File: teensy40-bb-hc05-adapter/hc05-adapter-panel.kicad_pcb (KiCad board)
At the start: 2 copper layers, 90.2 x 101.9 mm, 402 parts, among them J1 Conn_01x06_0.1_Header, J2 Conn_01x06_0.1_Socket, U1 74LVC1G17, U2 74LVC1G14

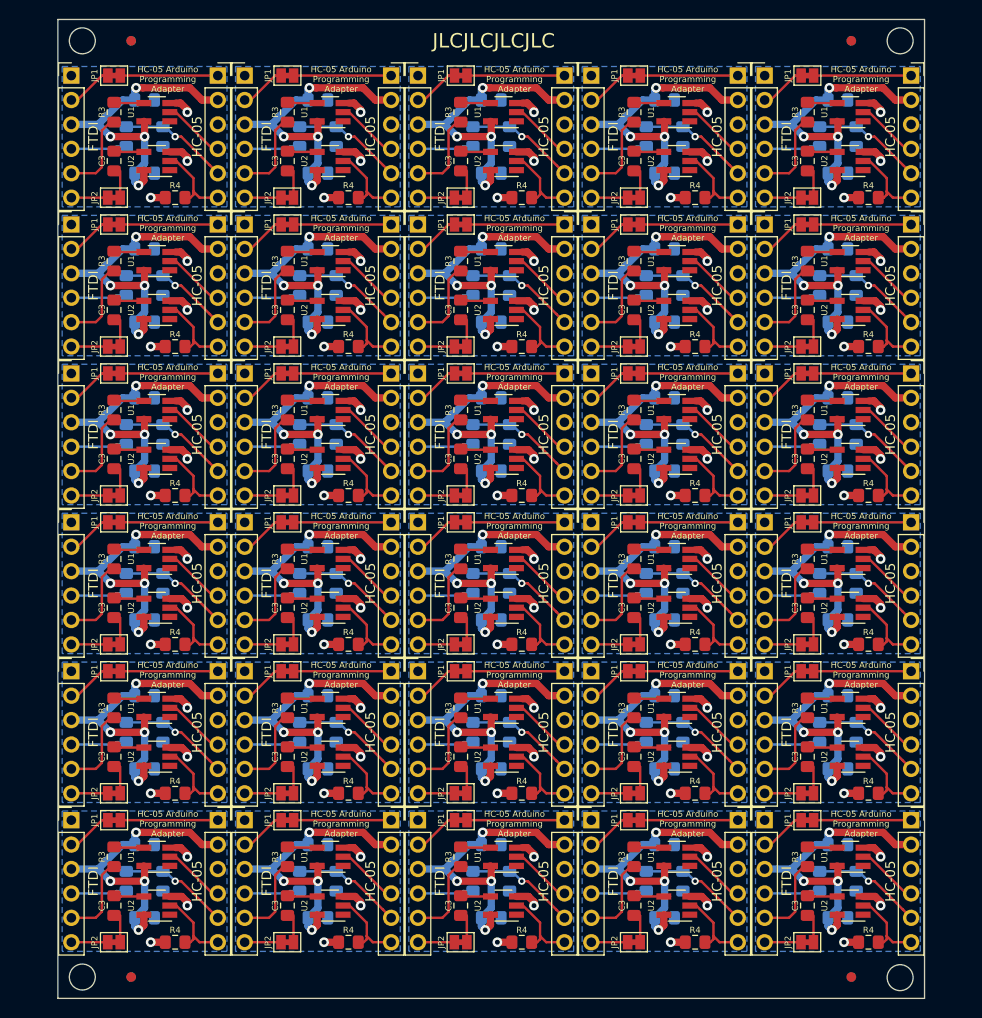
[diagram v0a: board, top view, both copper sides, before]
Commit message: Move edge rail to make less than 100mm long
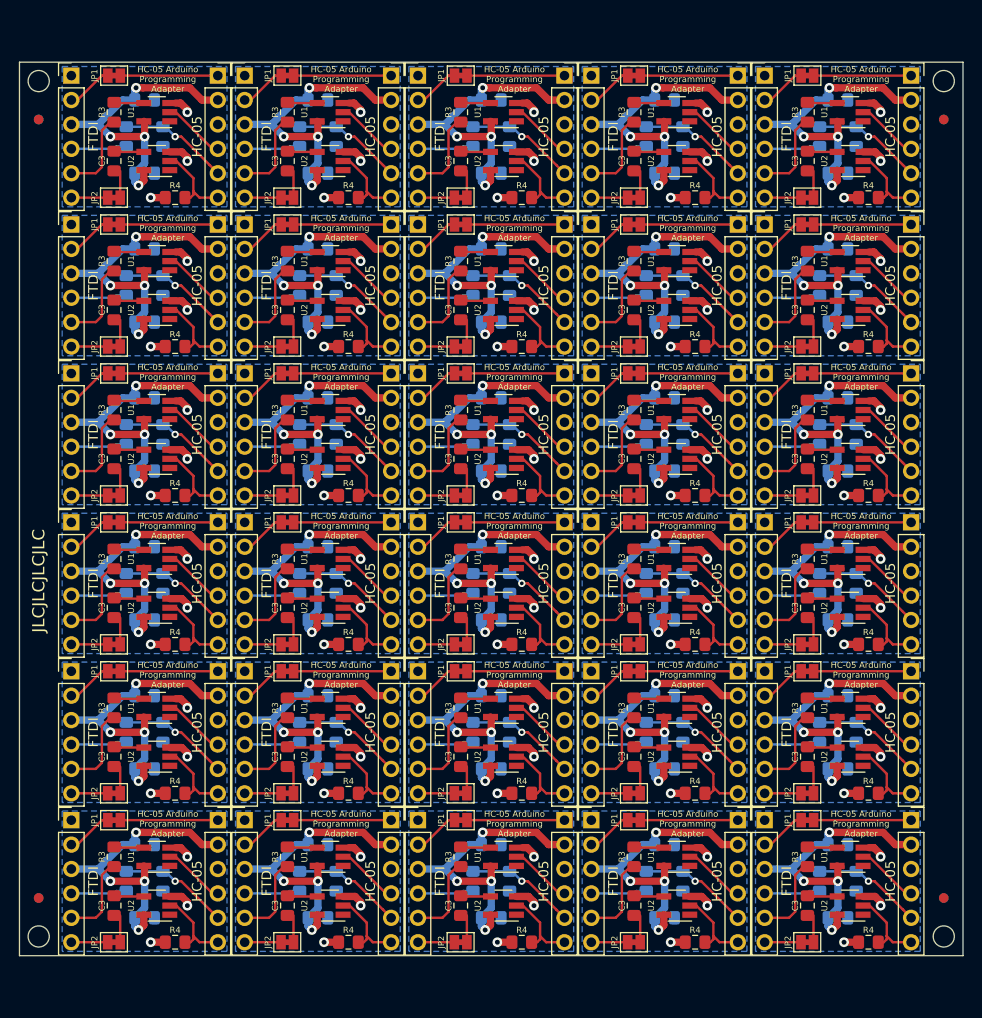
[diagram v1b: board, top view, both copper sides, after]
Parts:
- removed the REF** at (102.7, 138.7)
- removed the REF** at (182.8, 138.7) (x2)
- removed the REF** at (182.8, 41.3) (x2)
- removed the REF** at (107.8, 41.3) (x2)
- removed the REF** at (187.8, 138.8)
- removed the REF** at (187.8, 41.3)
- removed the REF** at (102.7, 41.3)
- removed the REF** at (107.8, 138.7) (x2)
- added REF**: Fiducial_1mm_Mask2mm, Fiducial:Fiducial_1mm_Mask2mm, B.Cu at (192.4, 49.5)
- added REF**: Fiducial_1mm_Mask2mm, Fiducial:Fiducial_1mm_Mask2mm, F.Cu at (98.2, 49.5)
- added REF**: MountingHole_2.2mm_M2, MountingHole:MountingHole_2.2mm_M2, F.Cu at (98.2, 134.5)
- added REF**: MountingHole_2.2mm_M2, MountingHole:MountingHole_2.2mm_M2, F.Cu at (98.2, 45.5)
- added REF**: Fiducial_1mm_Mask2mm, Fiducial:Fiducial_1mm_Mask2mm, B.Cu at (192.4, 130.5)
- added REF**: Fiducial_1mm_Mask2mm, Fiducial:Fiducial_1mm_Mask2mm, F.Cu at (192.4, 130.5)
- added REF**: Fiducial_1mm_Mask2mm, Fiducial:Fiducial_1mm_Mask2mm, F.Cu at (192.4, 49.5)
- added REF**: MountingHole_2.2mm_M2, MountingHole:MountingHole_2.2mm_M2, F.Cu at (192.4, 45.5)
- added REF**: MountingHole_2.2mm_M2, MountingHole:MountingHole_2.2mm_M2, F.Cu at (192.4, 134.5)
- added REF**: Fiducial_1mm_Mask2mm, Fiducial:Fiducial_1mm_Mask2mm, F.Cu at (98.2, 130.5)
- added REF**: Fiducial_1mm_Mask2mm, Fiducial:Fiducial_1mm_Mask2mm, B.Cu at (98.2, 130.5)
- added REF**: Fiducial_1mm_Mask2mm, Fiducial:Fiducial_1mm_Mask2mm, B.Cu at (98.2, 49.5)
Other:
- board size 90.2 x 101.9 mm -> 98.2 x 93 mm
- board text added: "EDGE GRID: 2.5 mil"
